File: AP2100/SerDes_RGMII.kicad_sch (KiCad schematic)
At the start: 10 parts

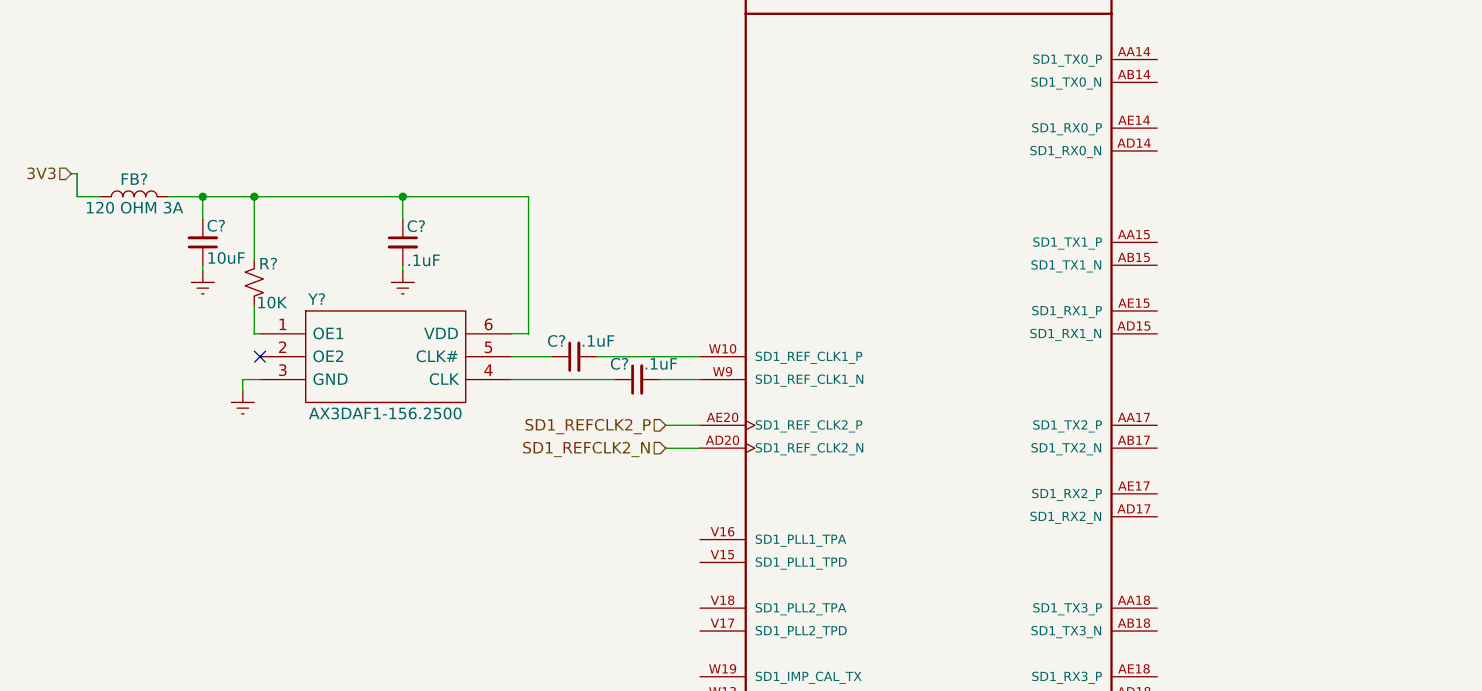
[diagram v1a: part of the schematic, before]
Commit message: Mostly done with USB - USB1 complete just duplicate to 2+3
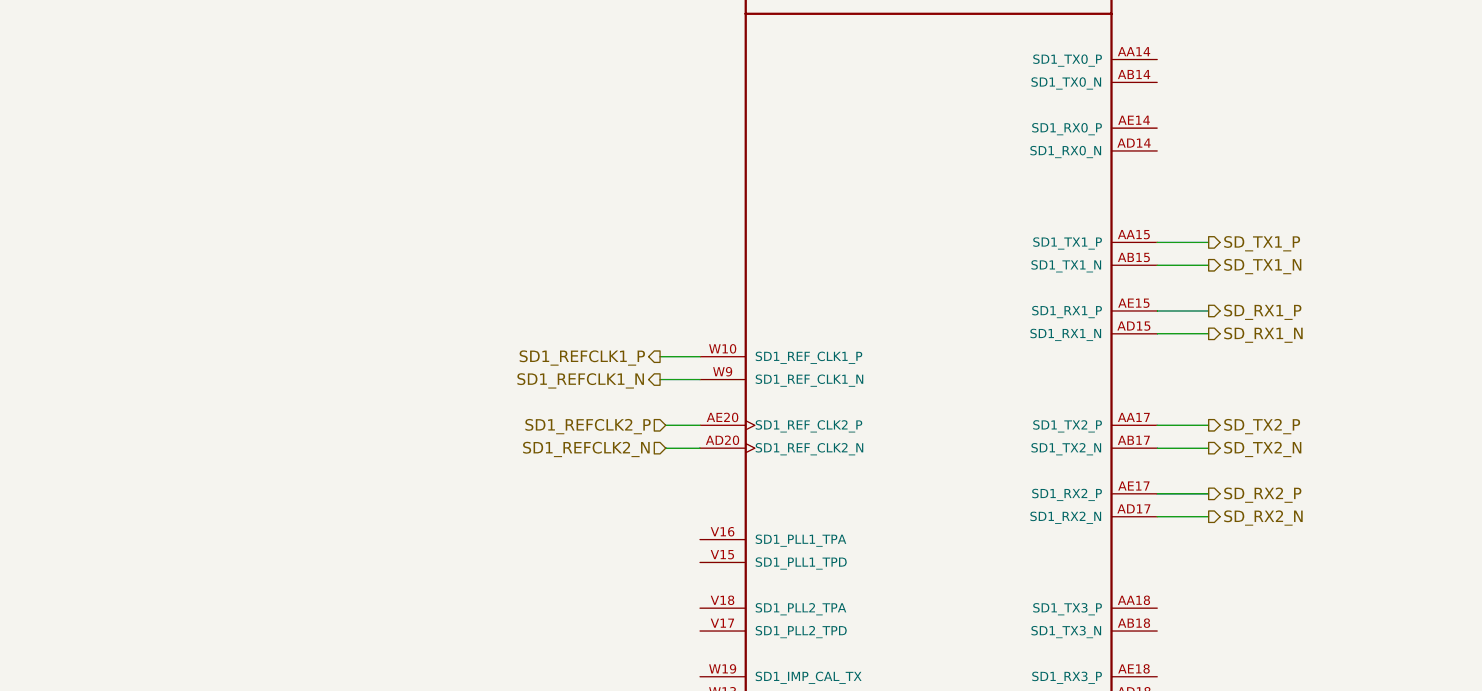
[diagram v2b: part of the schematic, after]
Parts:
- removed C? (x3): .1uF, Capacitor_SMD:C_0402_1005Metric, symbol Device:C_Small
- removed C?: 10uF, Capacitor_SMD:C_0805_2012Metric, symbol Device:C_Small
- removed FB?: 120 OHM 3A, Inductor_SMD:L_0603_1608Metric, symbol Device:L
- removed R?: 10K, Resistor_SMD:R_0402_1005Metric, symbol Device:R_Small_US
- removed Y?: AX3DAF1-156.2500, AX3DCF11562500, symbol AX3DCF1-156.2500:AX3DCF1-156.2500
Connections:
- net SD1_REFCLK1_N: now reaches U?.W9 (SD1_REF_CLK1_N)
- net SD_TX1_P: now reaches U?.AA15 (SD1_TX1_P)
- net SD_TX2_P: now reaches U?.AA17 (SD1_TX2_P)
- net SD_TX1_N: now reaches U?.AB15 (SD1_TX1_N)
- net SD_TX2_N: now reaches U?.AB17 (SD1_TX2_N)
- net SD_RX1_N: now reaches U?.AD15 (SD1_RX1_N)
- net SD_RX2_N: now reaches U?.AD17 (SD1_RX2_N)
- net SD_RX1_P: now reaches U?.AE15 (SD1_RX1_P)
- net SD_RX2_P: now reaches U?.AE17 (SD1_RX2_P)
- net SD1_REFCLK1_P: now reaches U?.W10 (SD1_REF_CLK1_P)
- no-connect marks 1 -> 0

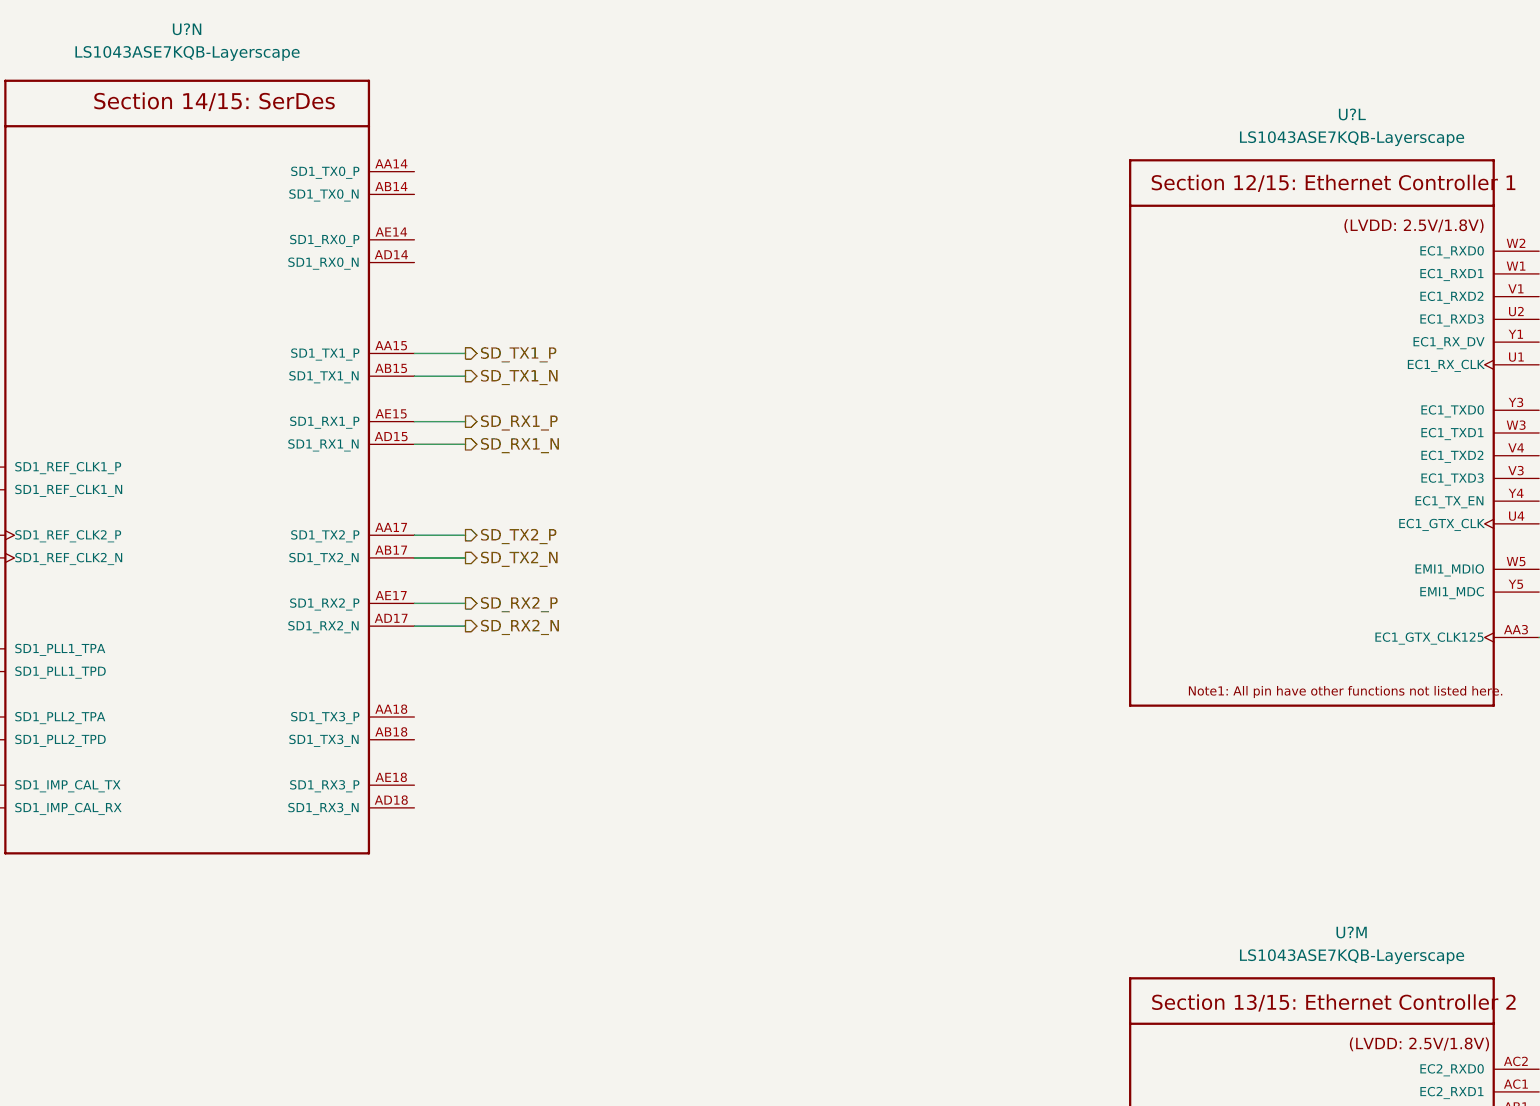
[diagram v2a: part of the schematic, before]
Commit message: Annotate and update PCB with current design
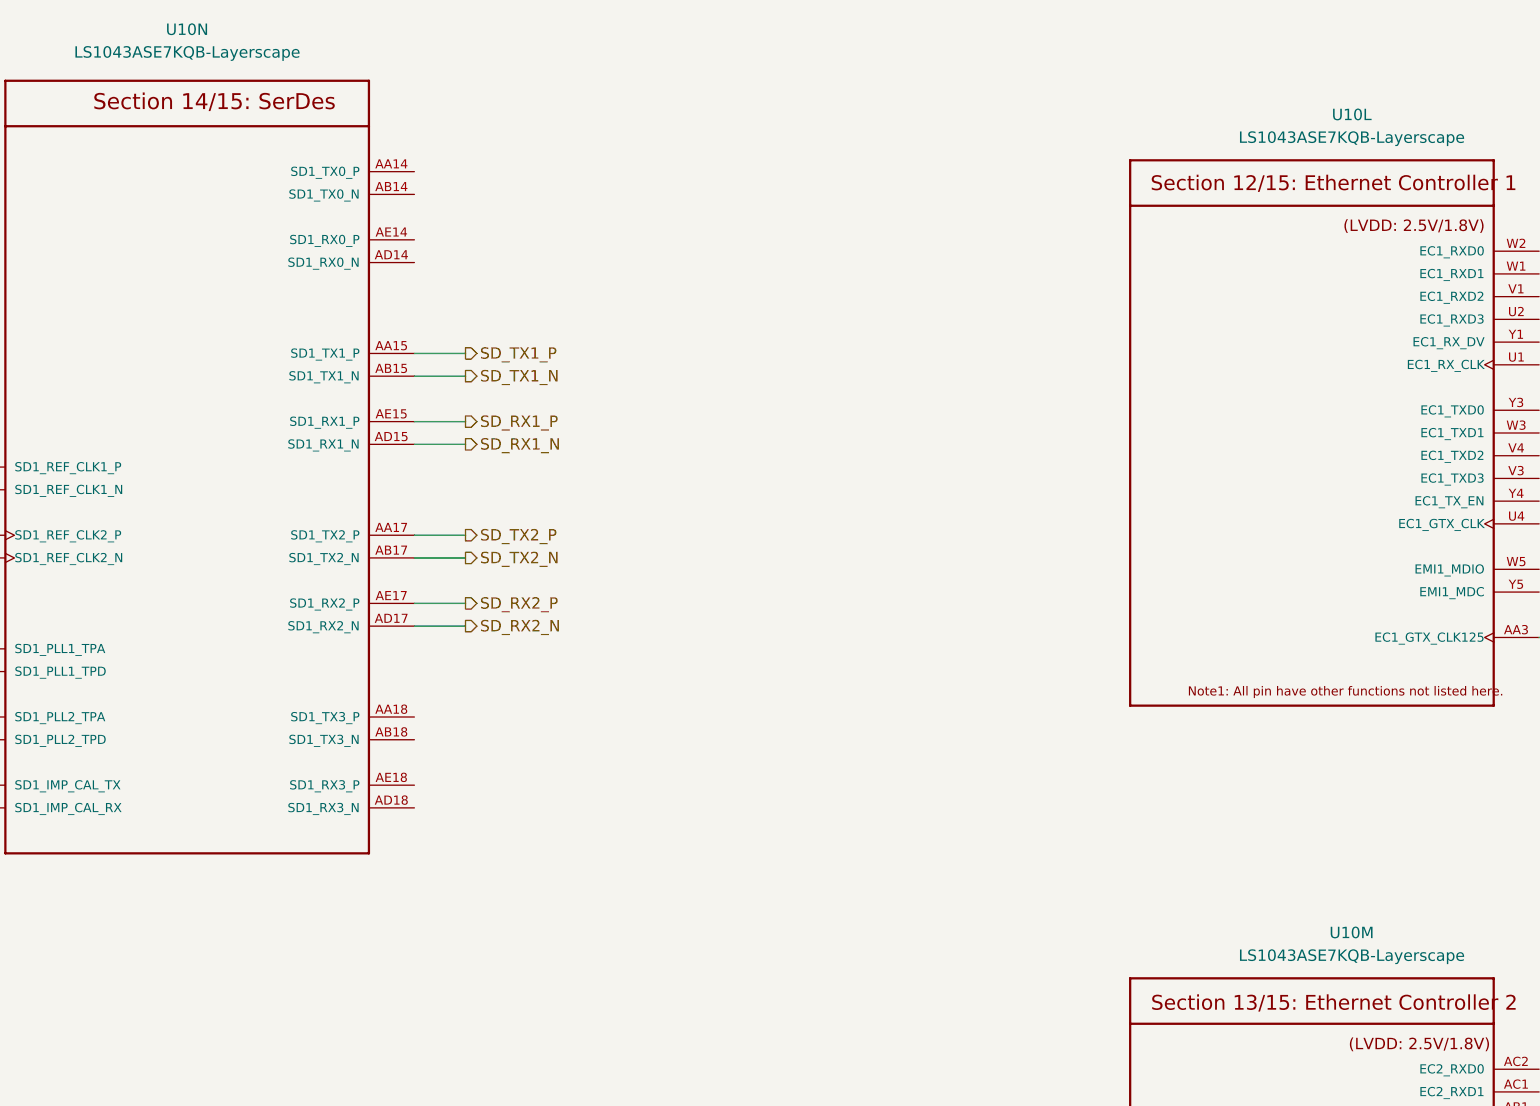
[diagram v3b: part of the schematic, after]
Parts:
- gave numbers to parts that had none: 1
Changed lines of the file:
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@@
   (symbol (lib_id "AP2100-rescue:LS1043ASE7KQB-Layerscape") (at 252.095 78.74 0) (unit 12)
     (in_bom yes) (on_board yes)
-    (property "Reference" "U?" (id 0) (at 255.27 41.91 0))
+    (property "Reference" "U10" (id 0) (at 255.27 41.91 0))
     (property "Value" "LS1043ASE7KQB-Layerscape" (id 1) (at 255.27 44.45 0))
     (property "Footprint" "PLS1043ASE7QQA:BGA621C80P25X25_2100X2100X192N" (id 2) (at 252.095 78.74 0)
@@
   (symbol (lib_id "AP2100-rescue:LS1043ASE7KQB-Layerscape") (at 248.285 167.64 0) (unit 13)
     (in_bom yes) (on_board yes)
-    (property "Reference" "U?" (id 0) (at 255.27 133.35 0))
+    (property "Reference" "U10" (id 0) (at 255.27 133.35 0))
     (property "Value" "LS1043ASE7KQB-Layerscape" (id 1) (at 255.27 135.89 0))
     (property "Footprint" "PLS1043ASE7QQA:BGA621C80P25X25_2100X2100X192N" (id 2) (at 248.285 167.64 0)
@@
   (symbol (lib_id "AP2100-rescue:LS1043ASE7KQB-Layerscape") (at 123.825 76.2 0) (unit 14)
     (in_bom yes) (on_board yes)
-    (property "Reference" "U?" (id 0) (at 125.095 32.385 0))
+    (property "Reference" "U10" (id 0) (at 125.095 32.385 0))
     (property "Value" "LS1043ASE7KQB-Layerscape" (id 1) (at 125.095 34.925 0))
     (property "Footprint" "PLS1043ASE7QQA:BGA621C80P25X25_2100X2100X192N" (id 2) (at 123.825 76.2 0)

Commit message: RGMII ethernet section almost complete for 1st port Finish USB
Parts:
- added C? (x3): 22uF, Capacitor_SMD:C_0805_2012Metric, symbol Device:C_Small
- added C? (x4): 10uF, Capacitor_SMD:C_0805_2012Metric, symbol Device:C_Small
- added C?: .1uF, Capacitor_SMD:C_0201_0603Metric, symbol Device:C_Small
- added IC?: KSZ9131RNXC, LIB_KSZ9131RNXC:QFN50P700X700X90-49N, symbol KSZ9131RNXC:KSZ9131RNXC
- added Q?: NTA4151P, Package_TO_SOT_SMD:SOT-416, symbol Device:Q_PMOS_GSD
- added R?: 330, Resistor_SMD:R_0402_1005Metric, symbol Device:R_Small_US
- added R? (x6): 22, Resistor_SMD:R_0402_1005Metric, symbol Device:R_Small_US
- added R? (x2): 1K, Resistor_SMD:R_0402_1005Metric, symbol Device:R_Small_US
- added R? (x2): 0, Resistor_SMD:R_0402_1005Metric, symbol Device:R_Small_US
- added R?: 100K, Resistor_SMD:R_0402_1005Metric, symbol Device:R_Small_US
- added R?: 6.04K, Resistor_SMD:R_0402_1005Metric, symbol Device:R_Small_US
- added R?: DNS 0, Resistor_SMD:R_0402_1005Metric, symbol Device:R_Small_US
- added R?: 26.1K, Resistor_SMD:R_0402_1005Metric, symbol Device:R_Small_US
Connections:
- net 25MHZ_EC1_RGMII: now also IC?.46 (XI); no longer U10.AA3 (EC1_GTX_CLK125)
- net at U10.U1 (EC1_RX_CLK): now also R?.1
- net at U10.U2 (EC1_RXD3): now also R?.1
- net at U10.U4 (EC1_GTX_CLK): now also IC?.24 (TXC)
- net at U10.V1 (EC1_RXD2): now also R?.1
- net at U10.V3 (EC1_TXD3): now also IC?.22 (TXD3)
- net at U10.V4 (EC1_TXD2): now also IC?.21 (TXD2)
- net at U10.W1 (EC1_RXD1): now also R?.1
- net at U10.W2 (EC1_RXD0): now also R?.1
- net at U10.W3 (EC1_TXD1): now also IC?.20 (TXD1)
- net at U10.W5 (EMI1_MDIO): now also IC?.37 (MDIO)
- net at U10.Y1 (EC1_RX_DV): now also R?.1
- net at U10.Y3 (EC1_TXD0): now also IC?.19 (TXD0)
- net at U10.Y4 (EC1_TX_EN): now also IC?.25 (TX_CTL)
- net at U10.Y5 (EMI1_MDC): now also IC?.36 (MDC)
- net 25MHZ_EC2_RGMII renamed 125M_CLK
- net 125M_CLK: now also U10.AA3 (EC1_GTX_CLK125)
- new net: C?.2, C?.2 (x3)
- new net: IC?.28 (RXD2/MODE2), R?.2
- new net: IC?.31 (RXD1/MODE1), R?.2
- new net: IC?.32 (RXD0/MODE0), R?.2
- new net: IC?.33 (RX_CTL/CLK125_EN), R?.1, R?.2
- new net: Q?.3 (D), R?.1
- new net: Q?.1 (G), R?.2
- new net: IC?.35 (RXC/PHYAD2), R?.2
- new net: IC?.27 (RXD3/MODE3), R?.2
- new net: IC?.42 (RESET_N), R?.2
- new net: IC?.48 (ISET), R?.1
- new net 3V3: IC?.1 (AVDDH_1), IC?.12 (AVDDH_2), IC?.16 (DVDDH_1), IC?.34 (DVDDH_2), IC?.40 (DVDDH_3), Q?.2 (S), R?.1, R?.1
- new net GND: C?.1, C?.1, C?.1, C?.1, C?.1, C?.1, IC?.29 (VSS), IC?.49 (P_VSS), R?.2, R?.2, R?.2
- new net GVDD: R?.1
- new net LDO_O: IC?.43 (LDO_O), R?.1
- new net SOC_IRQ0: IC?.38 (INT_N/PME_N2/ALLPHYAD), R?.2
- new net VDD_ETH: IC?.18 (DVDDL_1), IC?.23 (DVDDL_2), IC?.26 (DVDDL_3), IC?.30 (DVDDL_4), IC?.39 (DVDDL_5), IC?.4 (AVDDL_1), IC?.44 (AVDDL_PLL), IC?.9 (AVDDL_2), R?.2, R?.2
- no-connect marks 0 -> 4
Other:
- moved on the sheet: U10L, U10M, U10N

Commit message: Finish Ethernet all that's left is SerDes
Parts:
- removed C? (x3): 22uF, Capacitor_SMD:C_0805_2012Metric, symbol Device:C_Small
- removed C? (x4): 10uF, Capacitor_SMD:C_0805_2012Metric, symbol Device:C_Small
- removed C?: .1uF, Capacitor_SMD:C_0201_0603Metric, symbol Device:C_Small
- removed R?: 330, Resistor_SMD:R_0402_1005Metric, symbol Device:R_Small_US
- removed R?: 0, Resistor_SMD:R_0402_1005Metric, symbol Device:R_Small_US
- removed R?: DNS 0, Resistor_SMD:R_0402_1005Metric, symbol Device:R_Small_US
- removed R?: 26.1K, Resistor_SMD:R_0402_1005Metric, symbol Device:R_Small_US
- added C? (x4): .1uF, Capacitor_SMD:C_0402_1005Metric, symbol Device:C_Small
- added IC?: KSZ9131RNXC, LIB_KSZ9131RNXC:QFN50P700X700X90-49N, symbol KSZ9131RNXC:KSZ9131RNXC
- added J?: L836-1J1T-43, L836-1J1T-43:BEL_L836-1J1T-43, symbol L836-1J1T-43:L836-1J1T-43
- added Q?: NTA4151P, Package_TO_SOT_SMD:SOT-416, symbol Device:Q_PMOS_GSD
- added R? (x4): 220, Resistor_SMD:R_0402_1005Metric, symbol Device:R_Small_US
- added R? (x10): 10K, Resistor_SMD:R_0402_1005Metric, symbol Device:R_Small_US
- added R? (x6): DNP 10K, Resistor_SMD:R_0402_1005Metric, symbol Device:R_Small_US
- added R? (x8): DNP 1K, Resistor_SMD:R_0402_1005Metric, symbol Device:R_Small_US
- added R? (x8): 1K, Resistor_SMD:R_0402_1005Metric, symbol Device:R_Small_US
- added R? (x6): 22, Resistor_SMD:R_0402_1005Metric, symbol Device:R_Small_US
- added R?: 0, Resistor_SMD:R_0402_1005Metric, symbol Device:R_Small_US
- added R?: 100K, Resistor_SMD:R_0402_1005Metric, symbol Device:R_Small_US
- added R?: 6.04K, Resistor_SMD:R_0402_1005Metric, symbol Device:R_Small_US
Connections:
- net VDD_ETH is gone; now on an unnamed net: IC?.18 (DVDDL_1), IC?.23 (DVDDL_2), IC?.26 (DVDDL_3), IC?.30 (DVDDL_4), IC?.39 (DVDDL_5), IC?.4 (AVDDL_1), IC?.44 (AVDDL_PLL), IC?.9 (AVDDL_2)
- net 3V3: now also R?.2, IC?.1 (AVDDH_1), IC?.12 (AVDDH_2), IC?.16 (DVDDH_1), IC?.34 (DVDDH_2), IC?.40 (DVDDH_3), J?.14, J?.16, Q?.2 (S), R?.1, R?.1, R?.1, R?.1, R?.1, R?.1, R?.1, R?.1, R?.1, R?.1, R?.1, R?.1, R?.1, R?.1, R?.1, R?.2, R?.2, R?.2; no longer R?.1
- net GND: now also C?.1, C?.1, C?.1, C?.1, IC?.29 (VSS), IC?.49 (P_VSS), J?.S1 (SHIELD), J?.S2 (SHIELD), R?.2, R?.2, R?.2, R?.2, R?.2, R?.2, R?.2, R?.2, R?.2, R?.2, R?.2, R?.2, R?.2, R?.2, R?.2, R?.2
- net P0_RXD2: now reaches IC?.28 (RXD2/MODE2), R?.2
- net P0_RXD2: now also R?.1, R?.2
- net P0_RXD1: now reaches IC?.31 (RXD1/MODE1), R?.2
- net P0_RXD1: now also R?.1, R?.2
- net P0_RXD0: now reaches IC?.32 (RXD0/MODE0), R?.2
- net P0_RXD0: now also R?.1, R?.2
- net P0_RX_CTL/CLK125_EN: now reaches IC?.33 (RX_CTL/CLK125_EN), R?.1, R?.2
- net P0_RX_CLK: now reaches IC?.35 (RXC/PHYAD2), R?.2
- net P0_RX_CLK: now also R?.1, R?.2
- net P0_RXD3: now reaches IC?.27 (RXD3/MODE3), R?.2
- net P0_RXD3: now also R?.1, R?.2
- net at IC?.42 (RESET_N): now also R?.1; no longer R?.2
- net at U10.AA1 (EC2_RX_CLK): now also R?.1
- net at U10.AA2 (EC2_RXD3): now also R?.1
- net at U10.AA4 (EC2_GTX_CLK): now also IC?.24 (TXC)
- net at U10.AB1 (EC2_RXD2): now also R?.1
- net at U10.AB3 (EC2_TXD3): now also IC?.22 (TXD3)
- net at U10.AC1 (EC2_RXD1): now also R?.1
- net at U10.AC2 (EC2_RXD0): now also R?.1
- net at U10.AC3 (EC2_TXD2): now also IC?.21 (TXD2)
- net at U10.AC4 (EC2_TXD1): now also IC?.20 (TXD1)
- net at U10.AD2 (EC2_RX_DV): now also R?.1
- net at U10.AD3 (EC2_TXD0): now also IC?.19 (TXD0)
- net at U10.AE3 (EC2_TX_EN): now also IC?.25 (TX_CTL)
- net at U10.W6 (EMI2_MDIO): now also IC?.37 (MDIO)
- net at U10.Y6 (EMI2_MDC): now also IC?.36 (MDC)
- net ETH0_TD4_P: now reaches IC?.10 (TXRXP_D)
- net ETH0_TD4_N: now reaches IC?.11 (TXRXM_D)
- net P0_LED2: now reaches IC?.15 (LED2/PHYAD1)
- net P0_LED2: now also R?.1, R?.1, R?.2
- net P0_LED1: now reaches IC?.17 (LED1/PME_N1//PHYAD0)
- net P0_LED1: now also R?.1, R?.1, R?.2
- net ETH0_TD1_P: now reaches IC?.2 (TXRXP_A)
- net ETH0_TD1_N: now reaches IC?.3 (TXRXM_A)
- net at IC?.41 (CLK125_NDO/LED_MODE): now also R?.1
- net ETH0_TD2_P: now reaches IC?.5 (TXRXP_B)
- net ETH0_TD2_N: now reaches IC?.6 (TXRXM_B)
- net ETH0_TD3_P: now reaches IC?.7 (TXRXP_C)
- net ETH0_TD3_N: now reaches IC?.8 (TXRXM_C)
- net LDO_O: no longer names the net of IC?.43 (LDO_O), R?.1
- new net: C?.2, J?.1 (TRCT3)
- new net: J?.17, R?.2
- new net: IC?.43 (LDO_O), R?.1
- new net: Q?.1 (G), R?.2
- new net: IC?.10 (TXRXP_D), J?.8 (TRD4+)
- new net: IC?.11 (TXRXM_D), J?.9 (TRD4-)
- new net: IC?.18 (DVDDL_1), IC?.23 (DVDDL_2), IC?.26 (DVDDL_3), IC?.30 (DVDDL_4), IC?.39 (DVDDL_5), IC?.4 (AVDDL_1), IC?.44 (AVDDL_PLL), IC?.9 (AVDDL_2), Q?.3 (D)
- new net: IC?.2 (TXRXP_A), J?.11 (TRD1+)
- new net: IC?.3 (TXRXM_A), J?.10 (TRD1-)
- new net: IC?.41 (CLK125_NDO/LED_MODE), R?.1
- new net: IC?.42 (RESET_N), R?.1
- new net: IC?.48 (ISET), R?.1
- new net: IC?.5 (TXRXP_B), J?.4 (TRD2+)
- new net: IC?.6 (TXRXM_B), J?.5 (TRD2-)
- new net: IC?.7 (TXRXP_C), J?.3 (TRD3+)
- new net: IC?.8 (TXRXM_C), J?.2 (TRD3-)
- new net: C?.2, J?.12 (TRCT1)
- new net: J?.13, R?.2
- new net: C?.2, J?.6 (TRCT2)
- new net: C?.2, J?.7 (TRCT4)
- new net 25MHZ_EC2_RGMII: IC?.46 (XI)
- new net ETH0_LED1-: R?.2
- new net ETH0_LED2-: R?.2
- new net P1_LED1: IC?.17 (LED1/PME_N1//PHYAD0), R?.1, R?.1, R?.2
- new net P1_LED2: IC?.15 (LED2/PHYAD1), R?.1, R?.1, R?.2
- new net P1_RXD0: IC?.32 (RXD0/MODE0), R?.1, R?.2, R?.2
- new net P1_RXD1: IC?.31 (RXD1/MODE1), R?.1, R?.2, R?.2
- new net P1_RXD2: IC?.28 (RXD2/MODE2), R?.1, R?.2, R?.2
- new net P1_RXD3: IC?.27 (RXD3/MODE3), R?.1, R?.2, R?.2
- new net P1_RX_CLK: IC?.35 (RXC/PHYAD2), R?.1, R?.2, R?.2
- new net P1_RX_CTL/CLK125_EN: IC?.33 (RX_CTL/CLK125_EN), R?.1, R?.2
- new net SOC_IRQ1: IC?.38 (INT_N/PME_N2/ALLPHYAD), R?.2
- no-connect marks 4 -> 9
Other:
- note added: "Mode [3:0] Description 1000 10/100 Full and Half, 1000BT Full (RGMII), PME Enable on LED1 1010 10/100 Full and Half, 1000BT Full (RGMII), PME Enable on INT_N 1100 1000BT Full (RGMII) 1110 10/100 Full and Half, 1000BT Full (RGMII)"
- note added: "NOTE: 125MHz Output Clock is Disabled"
- note added: "NOTE: LED Mode is Individual"
- note added: "NOTE: Mode is 1110 = 10/100 F/H, 1000BT Full (RGMII)"
- note added: "NOTE: PHY Address is 01h"
- note added: "NOTE: PHY Address is 02h"
- moved on the sheet: IC?, Q?, R?, U10L, U10M, U10N
